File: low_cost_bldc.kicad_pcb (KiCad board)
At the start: 4 copper layers, 40 x 40 mm, 79 parts, among them P1 USB_C_Plug_USB2.0, Q1 HSCB3014, Q2 HSCB3014, Q3 HSCB3014, Q4 HSCB3014, Q5 HSCB3014, Q6 HSCB3014, U1 CH32V003FxPx, U2 MT6701CT, U3 U2115C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

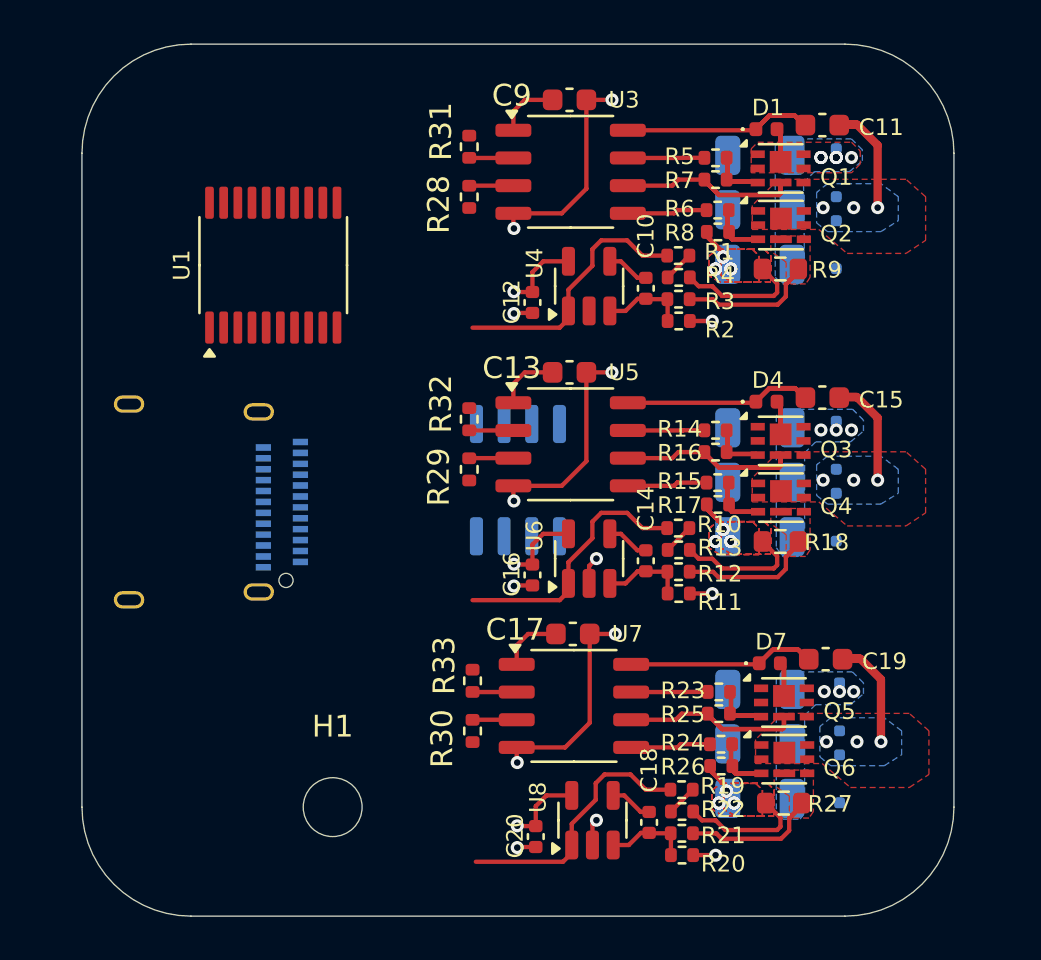
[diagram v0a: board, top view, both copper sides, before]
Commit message: Initial mounting holes, power lugs. Sitting at  @ qty 10 BOM estimate. Still need 12V, 3.3V power; comms connectors
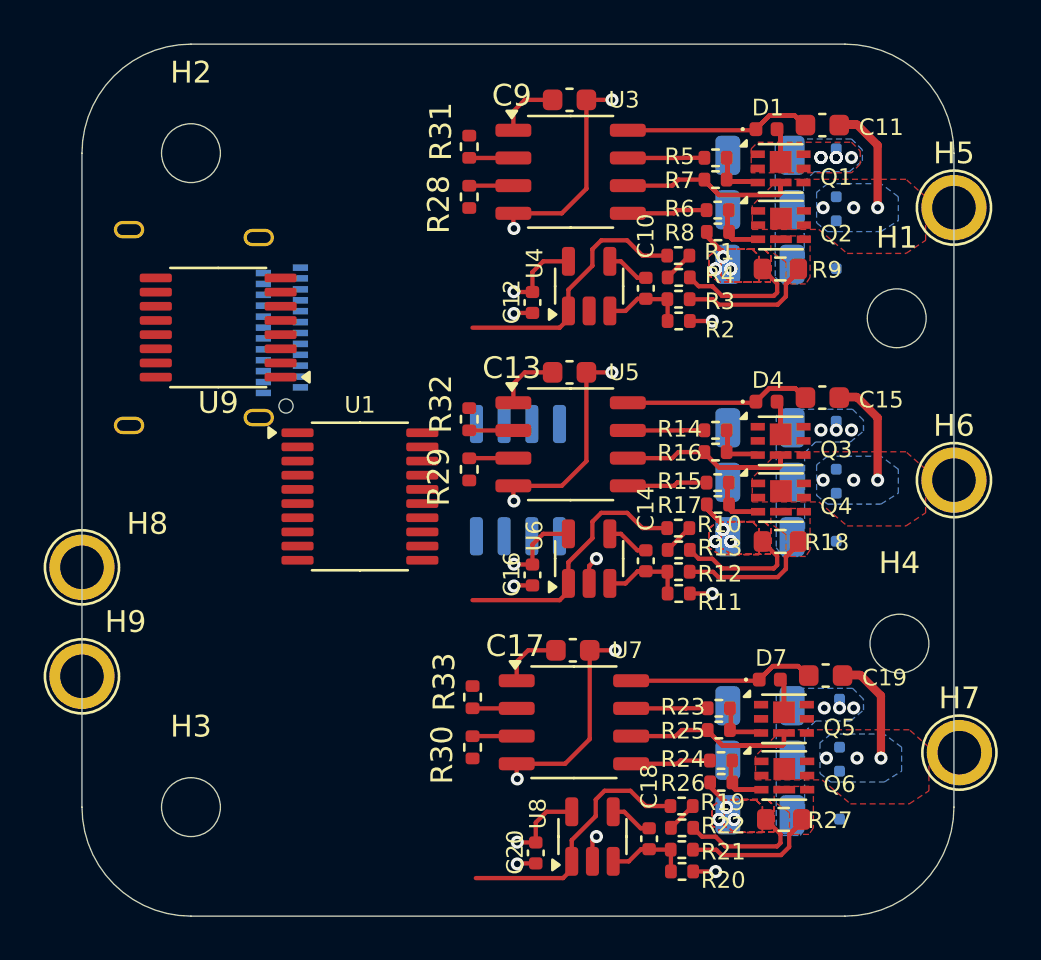
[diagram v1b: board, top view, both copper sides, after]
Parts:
- added H2: MountingHole, MountingHole:MountingHole_2.7mm_M2.5, F.Cu at (240.0, 145.0)
- added H3: MountingHole, MountingHole:MountingHole_2.7mm_M2.5, F.Cu at (240.0, 175.0)
- added H4: MountingHole, MountingHole:MountingHole_2.7mm_M2.5, F.Cu at (272.5, 167.5)
- added H5: MountingHole_Pad, TestPoint:TestPoint_Plated_Hole_D2.0mm, F.Cu at (275.0, 147.5)
- added H6: MountingHole_Pad, TestPoint:TestPoint_Plated_Hole_D2.0mm, F.Cu at (275.0, 160.0)
- added H7: MountingHole_Pad, TestPoint:TestPoint_Plated_Hole_D2.0mm, F.Cu at (275.2, 172.5)
- added H8: MountingHole_Pad, TestPoint:TestPoint_Plated_Hole_D2.0mm, F.Cu at (235.0, 164.0)
- added H9: MountingHole_Pad, TestPoint:TestPoint_Plated_Hole_D2.0mm, F.Cu at (235.0, 169.0)
- added U9: IP2721, Package_SO:TSSOP-16_4.4x5mm_P0.65mm, F.Cu at (241.2, 153.0)
- moved H1 34.2 mm to (272.4, 152.6)
- moved U1 11.3 mm to (247.8, 160.8), turned to 0 degrees
- moved P1 8.00 mm to (240.0, 153.0)
- moved C17 0.75 mm to (257.5, 167.8)
- moved C18 0.75 mm to (261.0, 176.4)
- moved C19 0.75 mm to (269.1, 169.0)
- moved C20 0.75 mm to (255.8, 177.1)
- moved C21 0.75 mm to (266.1, 175.3)
- moved C7 0.75 mm to (266.1, 170.3)
- moved C8 0.75 mm to (266.1, 172.8)
- moved D7 0.75 mm to (266.6, 169.2)
- moved D8 0.75 mm to (269.8, 171.2)
- moved D9 0.75 mm to (269.8, 174.4)
- moved Q5 0.75 mm to (267.2, 170.9)
- moved Q6 0.75 mm to (267.2, 173.6)
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
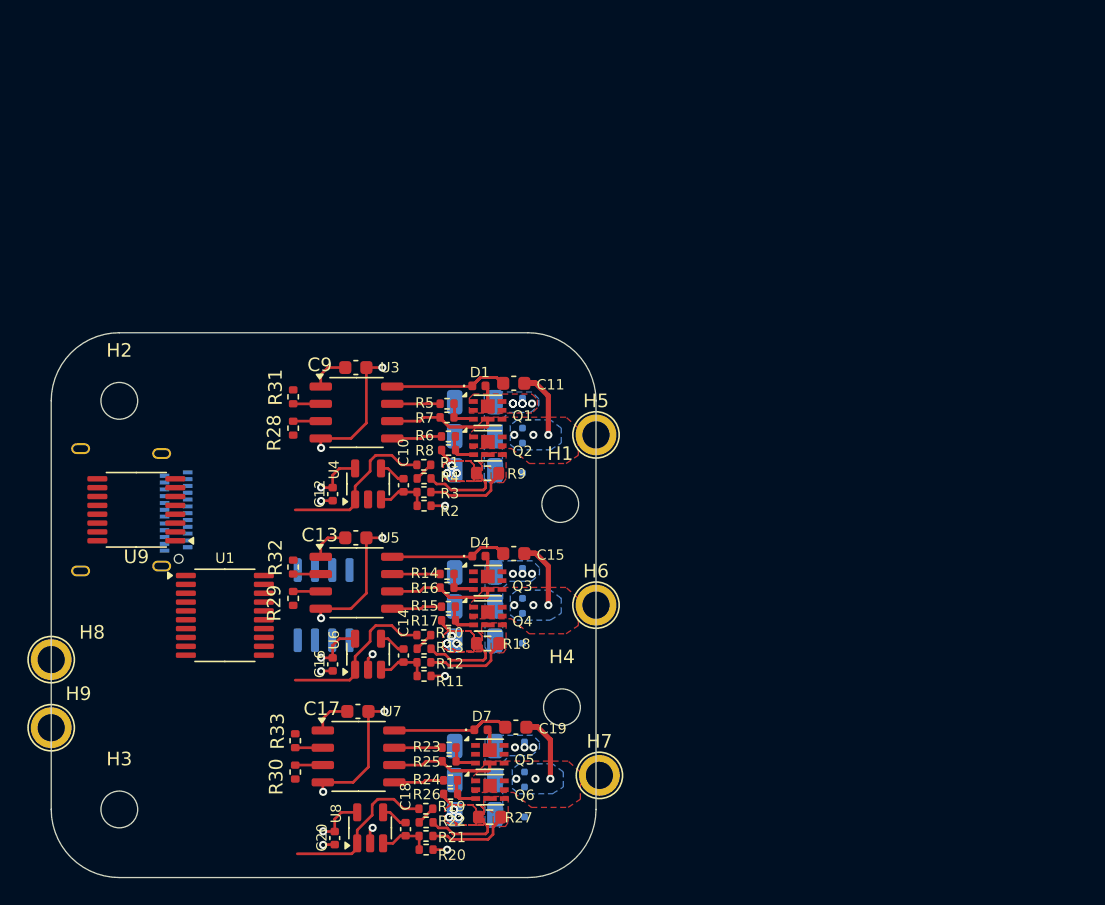
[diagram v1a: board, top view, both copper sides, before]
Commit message: Readme, rough connector placement, inverter refinement, increase MCU pin count to have a chance of succeeding.
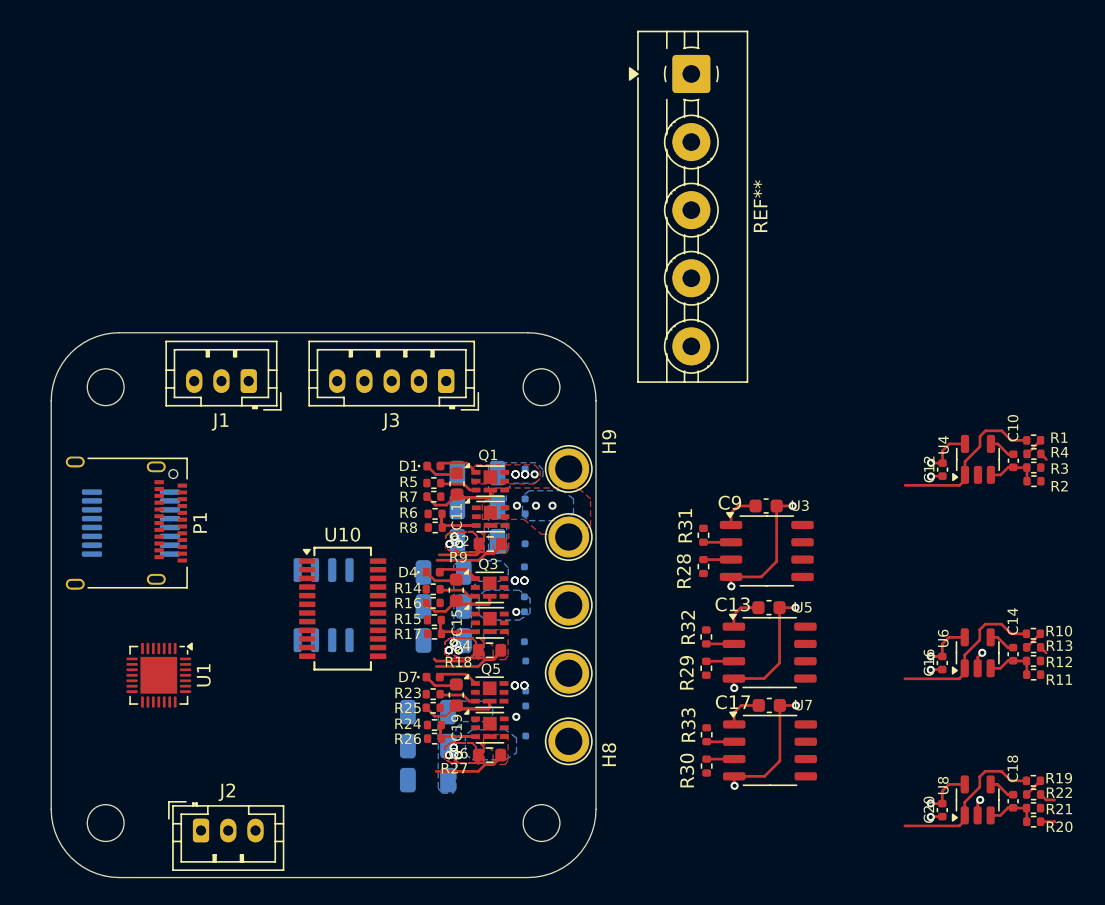
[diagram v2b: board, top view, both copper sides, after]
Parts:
- added J1: Conn_01x03, Connector_JST:JST_PH_B3B-PH-K_1x03_P2.00mm_Vertical, F.Cu at (249.5, 143.6)
- added J2: Conn_01x03, Connector_JST:JST_PH_B3B-PH-K_1x03_P2.00mm_Vertical, F.Cu at (246.0, 176.6)
- added J3: Conn_01x05, Connector_JST:JST_PH_B5B-PH-K_1x05_P2.00mm_Vertical, F.Cu at (264.0, 143.6)
- added REF**: TerminalBlock_MaiXu_MX126-5.0-05P_1x05_P5.00mm, TerminalBlock:TerminalBlock_MaiXu_MX126-5.0-05P_1x05_P5.00mm, F.Cu at (282.0, 121.0)
- added U10: UC6310, Package_SO:SSOP-24_3.9x8.7mm_P0.635mm, F.Cu at (256.4, 160.3)
- P1: moved to F.Cu
- U1: value CH32V003FxPx -> CH32V203GxUx; footprint Package_SO:TSSOP-20_4.4x6.5mm_P0.65mm -> Package_DFN_QFN:QFN-28-1EP_4x4mm_P0.4mm_EP2.7x2.7mm
- U9: moved to B.Cu
- moved C12 44.8 mm to (300.4, 150.1)
- moved C10 44.8 mm to (305.6, 149.4)
- moved R1 44.8 mm to (307.1, 147.9)
- moved R2 44.8 mm to (307.2, 150.9)
- moved R3 44.8 mm to (307.1, 149.9)
- moved R4 44.8 mm to (307.2, 148.9)
- moved U4 44.8 mm to (303.0, 149.3)
- moved C14 44.8 mm to (305.6, 163.6)
- moved R11 44.8 mm to (307.1, 165.1)
- moved R12 44.8 mm to (307.1, 164.1)
- moved R13 44.8 mm to (307.1, 163.1)
- moved U6 44.8 mm to (303.0, 163.5)
- moved C16 44.8 mm to (300.4, 164.2)
- moved R10 44.8 mm to (307.1, 162.1)
- moved C18 44.7 mm to (305.6, 174.4)
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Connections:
- U1 pad 16: unconnected-(U1-PC6-Pad16) -> Net-(U1-VSS-Pad16)
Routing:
- net GND: track 63.9 -> 46.3 mm, vias 32 -> 19
- net Net-(D7-K): track 13.7 -> 2.91 mm
- net Net-(D4-K): track 13.7 -> 2.91 mm
- net Net-(D1-K): track 13.7 -> 2.91 mm
- net /PHASE_V: track 18.2 -> 9.51 mm, vias 3 -> 1
- net /PHASE_U: track 18.2 -> 9.51 mm
- net /PHASE_W: track 18.2 -> 9.51 mm, vias 3 -> 1
- net VBUS: track 14.1 -> 8.95 mm, vias 13 -> 29
- net Net-(U3-LO): track 3.68 -> 0.00 mm
- net Net-(U5-LO): track 3.68 -> 0.00 mm
- net Net-(U7-LO): track 3.68 -> 0.00 mm
- net Net-(U7-HO): track 3.52 -> 0.00 mm
- net Net-(U5-HO): track 3.52 -> 0.00 mm
- net Net-(U3-HO): track 3.52 -> 0.00 mm
- net Net-(Q3-G): track 4.91 -> 2.61 mm
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- removed copper zone on F.Cu, net /PHASE_V
- removed copper zone on F.Cu, net /PHASE_W

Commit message: Organizing
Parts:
- added REF**: DFN-10-1EP_3x3mm_P0.5mm_EP1.55x2.48mm, Package_DFN_QFN:DFN-10-1EP_3x3mm_P0.5mm_EP1.55x2.48mm, F.Cu at (296.1, 157.0)
- moved C21 4.29 mm to (266.2, 170.5)
- moved C7 4.29 mm to (266.2, 165.5)
- moved C8 4.29 mm to (266.2, 168.0)
- moved C2 2.47 mm to (266.2, 158.0)
- moved C3 2.47 mm to (266.2, 160.5)
- moved C6 2.47 mm to (266.2, 163.0)
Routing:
- net GND: track 46.3 -> 48.6 mm

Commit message: Re-save pcbdoc
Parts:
- moved J2 38.6 mm to (265.0, 143.0), turned to 180 degrees
- moved J3 31.9 mm to (238.8, 163.0), turned to -90 degrees
- moved P1 24.6 mm to (253.5, 174.3), turned to 0 degrees
- moved U9 22.9 mm to (253.5, 173.1), turned to -90 degrees
- moved REF** 3.51 mm to (285.5, 120.8)
- moved U1 2.43 mm to (245.3, 165.2)
- moved J1 0.74 mm to (249.0, 143.0)
